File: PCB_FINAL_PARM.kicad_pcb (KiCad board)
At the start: 2 copper layers, 87.6 x 95.2 mm, 48 parts, among them J1 Conn_01x02_Servo1, J10 Conn_01x04_TRIS, J11 Conn_01x04_3v3, J2 Conn_01x03_UART1, J3 Conn_01x03_UART2, J4 Conn_01x04_PWM, J5 Conn_01x05_PROGRAMER, J6 Conn_01x02_POWER, J7 Conn_01x02_Servo2, J8 Conn_01x02_Servo3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

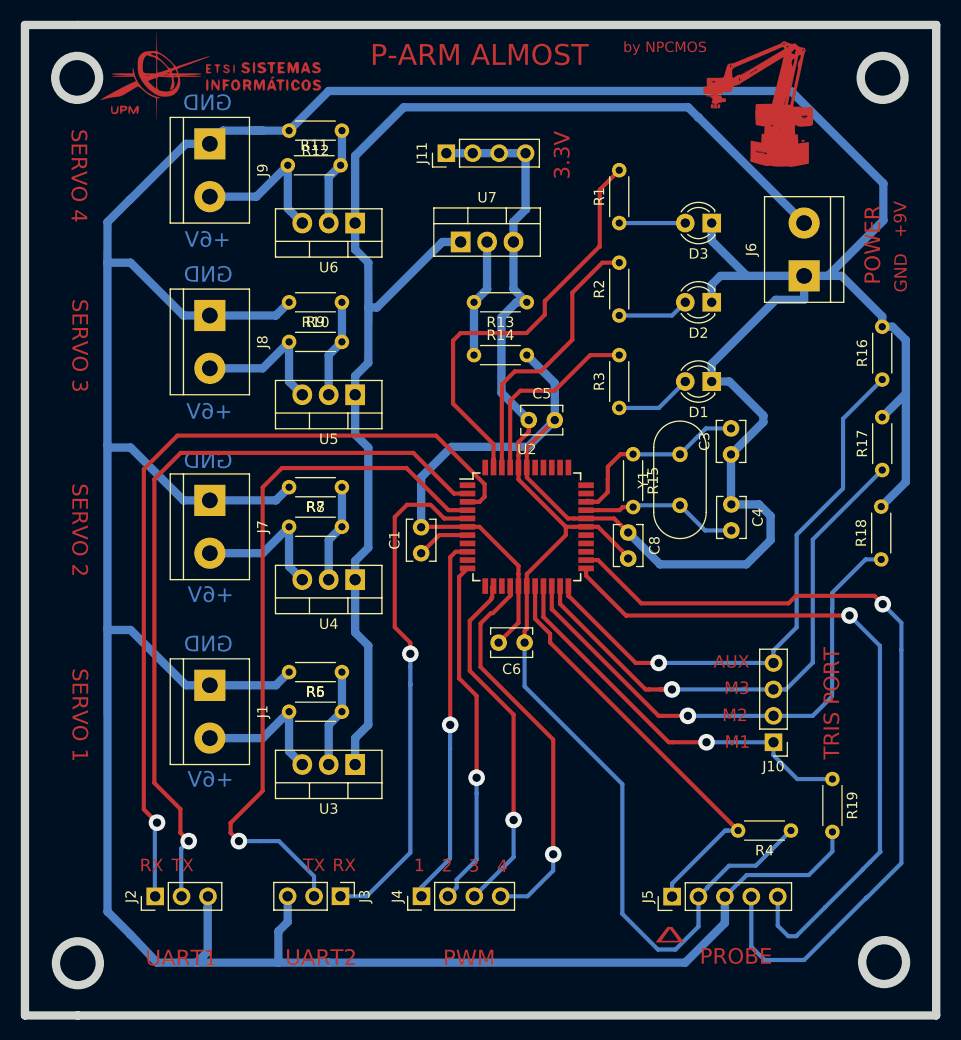
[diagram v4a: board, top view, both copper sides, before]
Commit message: Pasadas comprobaciones de HW y modificaciones con respecto a la sonda
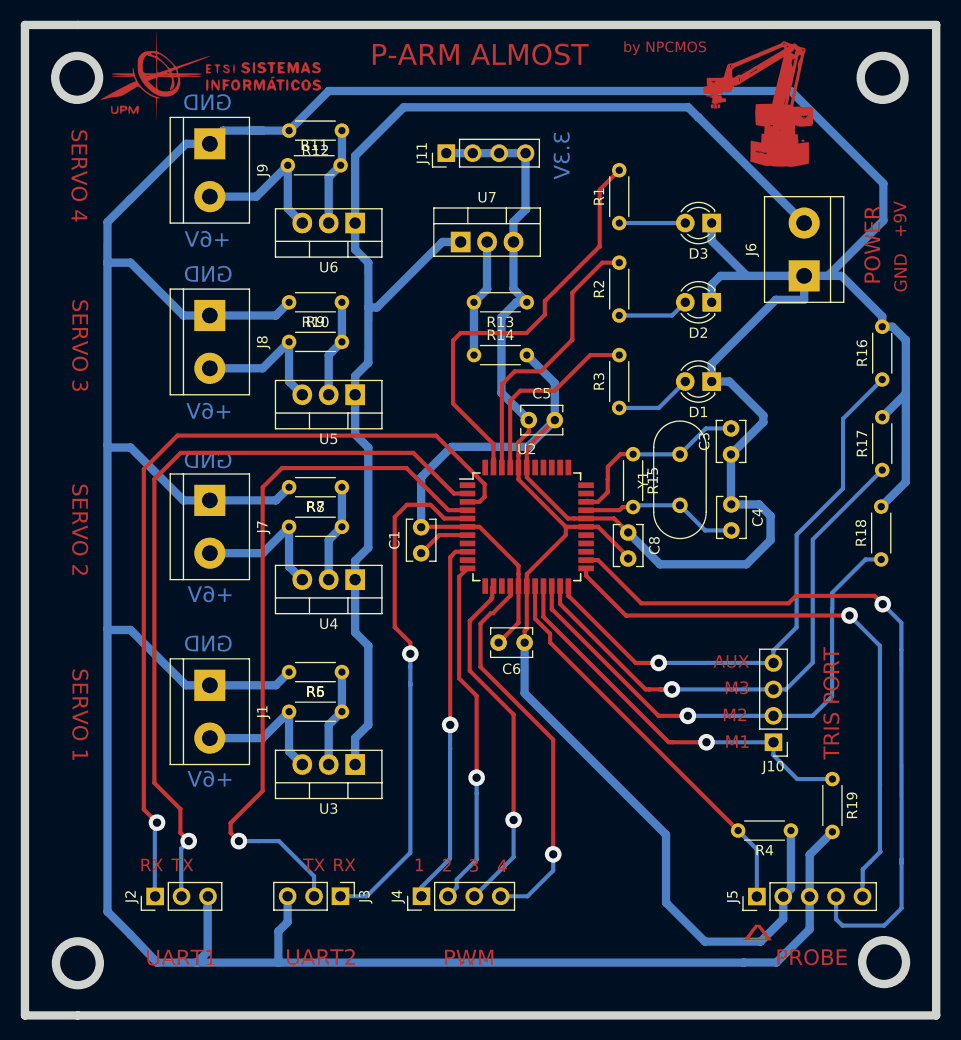
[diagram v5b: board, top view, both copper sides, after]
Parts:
- moved J5 8.15 mm to (205.0, 142.2)
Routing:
- net Net-(J5-Pad5): track 68.1 -> 56.7 mm
- net Net-(J5-Pad4): track 80.4 -> 70.6 mm
- net Net-(J5-Pad1): track 41.3 -> 38.7 mm
- net GND: track 485.7 -> 487.3 mm
- net +3V3: track 123.8 -> 122.9 mm

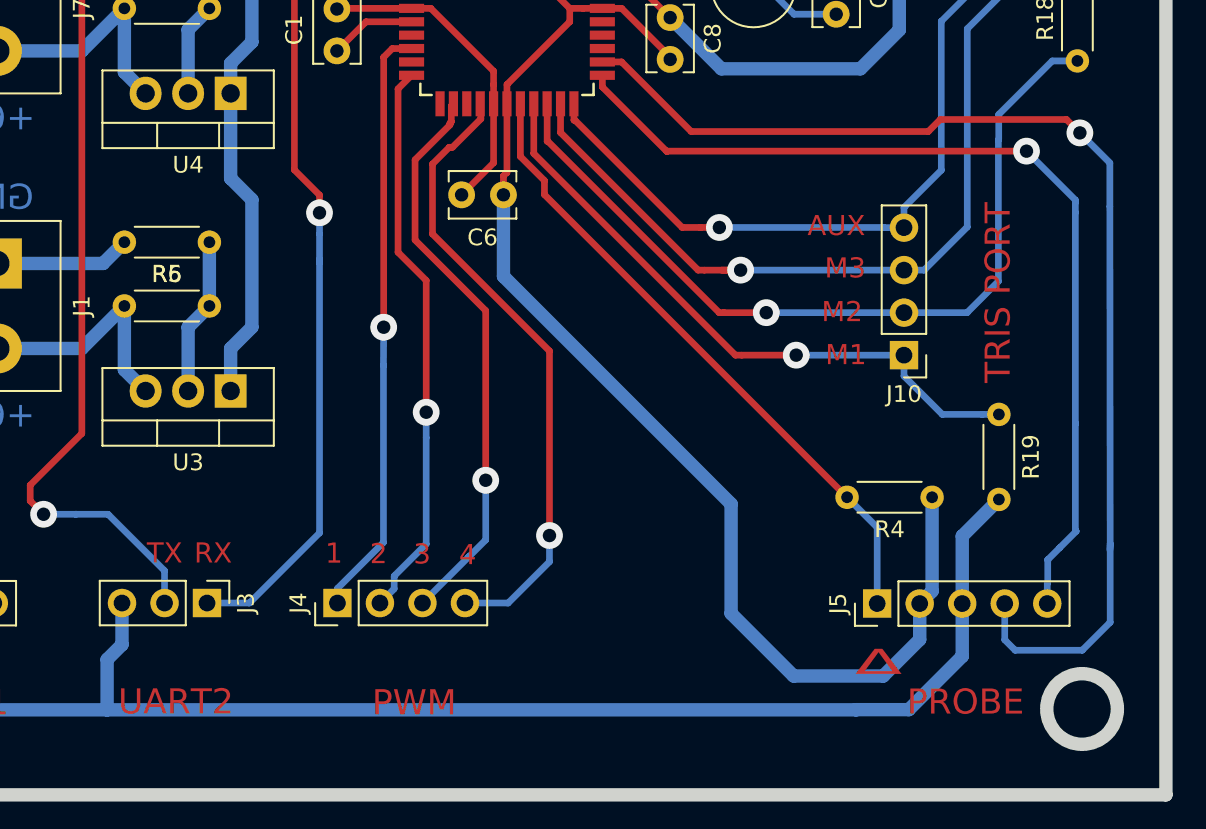
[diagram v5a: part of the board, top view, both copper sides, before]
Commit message: Aumentado el espacio para la sonda
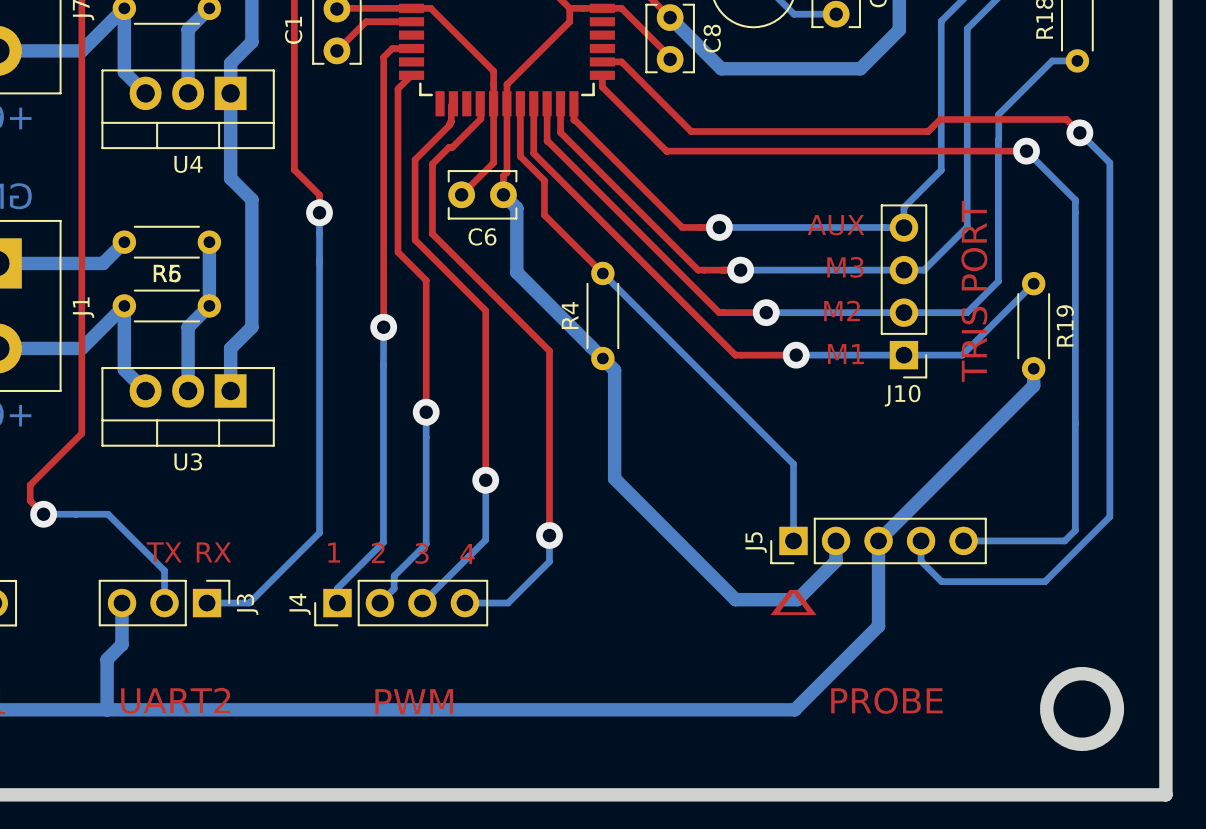
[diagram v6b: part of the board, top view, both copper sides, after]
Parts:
- moved R4 21.3 mm to (188.6, 127.6), turned to 90 degrees
- moved R19 8.08 mm to (214.3, 123.1)
- moved J5 6.24 mm to (200.0, 138.5)
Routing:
- net +3V3: track 122.9 -> 107.9 mm
- net Net-(J5-Pad1): track 38.7 -> 32.9 mm
- net GND: track 487.3 -> 492.0 mm
- net Net-(J5-Pad5): track 56.7 -> 58.5 mm
- net Net-(J10-Pad1): track 38.3 -> 39.9 mm
- net Net-(J5-Pad4): track 70.6 -> 69.2 mm

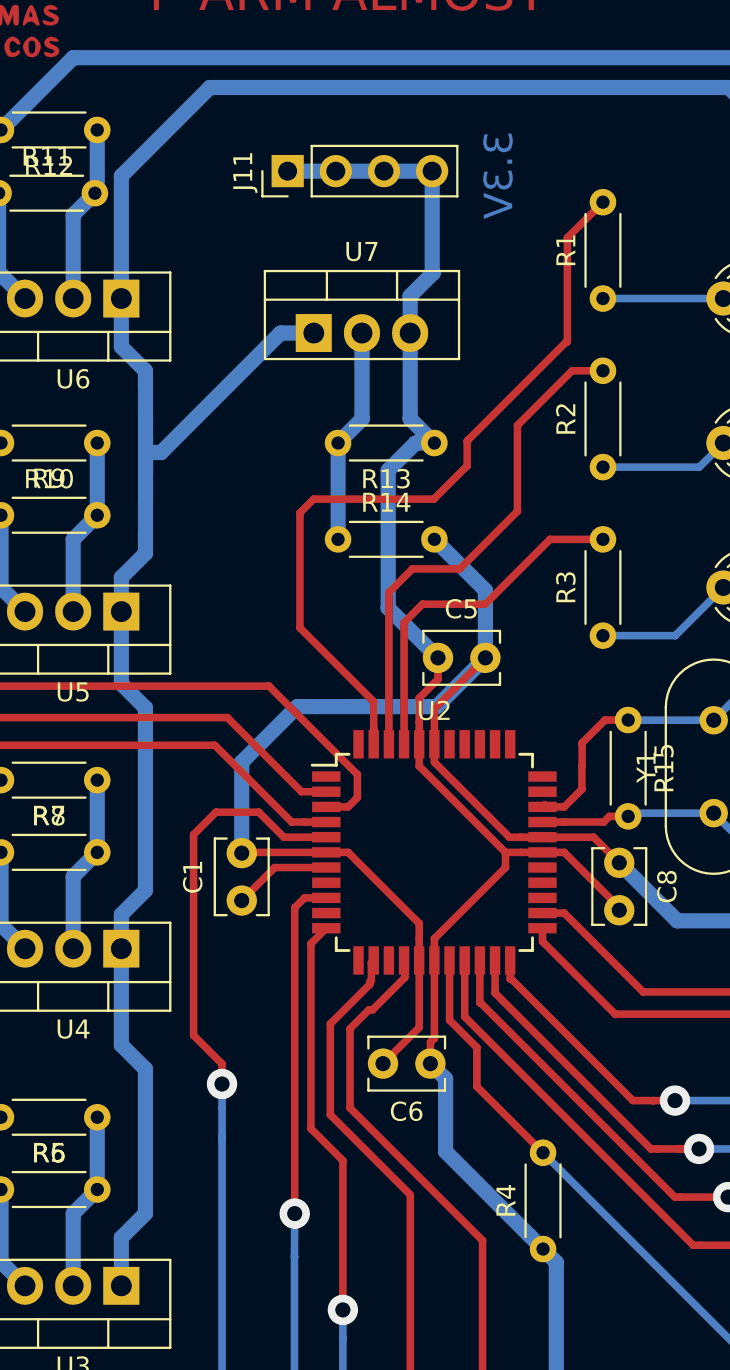
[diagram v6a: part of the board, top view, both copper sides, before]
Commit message: Sustituido el regulador del dspic
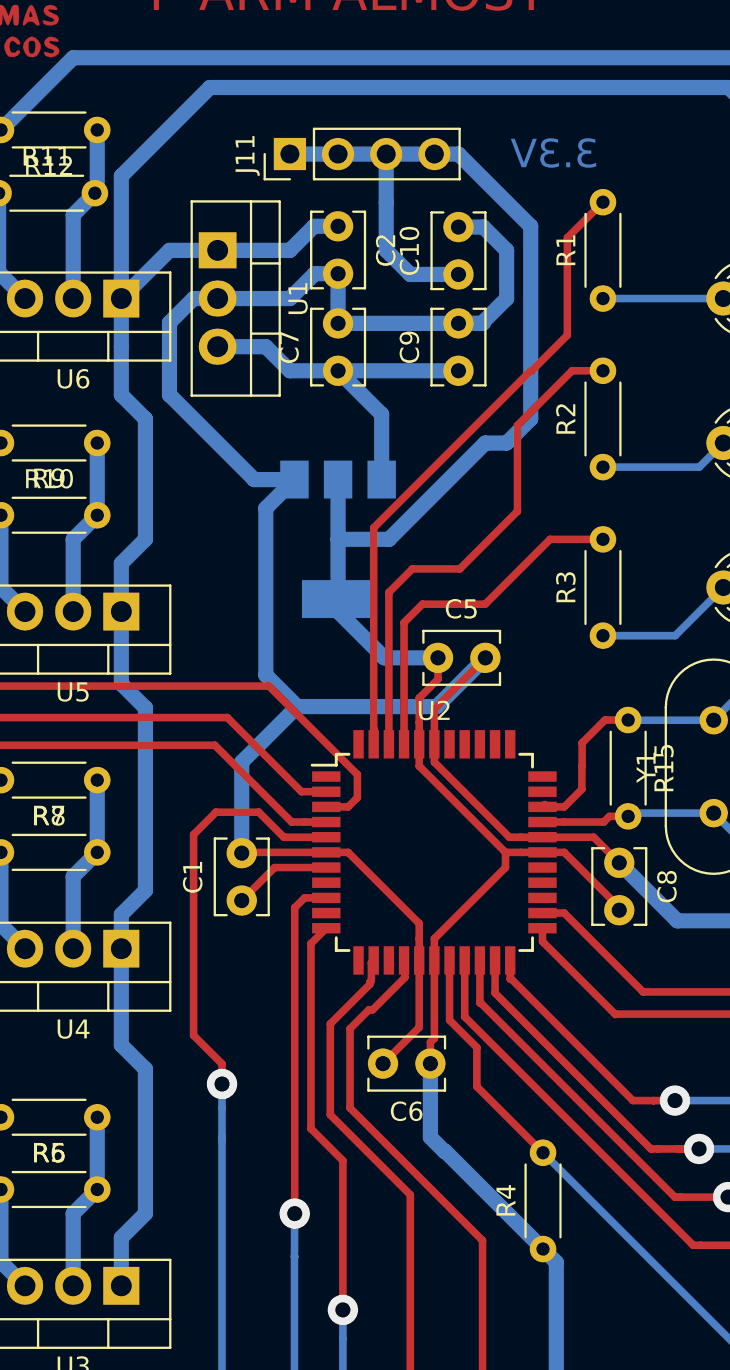
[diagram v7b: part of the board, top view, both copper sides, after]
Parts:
- removed R13: 240, Resistor_THT:R_Axial_DIN0204_L3.6mm_D1.6mm_P5.08mm_Horizontal
- removed R14: 400, Resistor_THT:R_Axial_DIN0204_L3.6mm_D1.6mm_P5.08mm_Horizontal
- added C10: 22uF, Capacitor_THT:C_Disc_D3.8mm_W2.6mm_P2.50mm, F.Cu at (184.2, 76.2)
- added C2: 0.33uF, Capacitor_THT:C_Disc_D3.8mm_W2.6mm_P2.50mm, F.Cu at (177.8, 73.7)
- added C7: 0.1uF, Capacitor_THT:C_Disc_D3.8mm_W2.6mm_P2.50mm, F.Cu at (177.8, 81.3)
- added C9: 10uF, Capacitor_THT:C_Disc_D3.8mm_W2.6mm_P2.50mm, F.Cu at (184.2, 81.3)
- added U1: L7805, Package_TO_SOT_THT:TO-220-3_Vertical, F.Cu at (171.4, 74.9)
- U7: value LM317T/DSPIC -> AZ1117-3.3; footprint Package_TO_SOT_THT:TO-220-3_Vertical -> Package_TO_SOT_SMD:SOT-223-3_TabPin2; moved to B.Cu
- moved U7 11.0 mm to (177.8, 90.2), turned to 270 degrees
- moved J11 0.91 mm to (175.3, 69.8)
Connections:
- J6 pad 2: Net-(J6-Pad2) -> Net-(C2-Pad1)
- U3 pad 1: Net-(J6-Pad2) -> Net-(C2-Pad1)
- U4 pad 1: Net-(J6-Pad2) -> Net-(C2-Pad1)
- U5 pad 1: Net-(J6-Pad2) -> Net-(C2-Pad1)
- U6 pad 1: Net-(J6-Pad2) -> Net-(C2-Pad1)
- U7 pad 1: Net-(J6-Pad2) -> GND
- U7 pad 2: Net-(R13-Pad2) -> +3V3
- U7 pad 3: +3V3 -> Net-(C7-Pad1)
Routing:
- net Net-(C2-Pad1): track 0.00 -> 124.4 mm
- net Net-(J6-Pad2): track 122.9 -> 0.00 mm
- net GND: track 492.0 -> 539.0 mm
- net +3V3: track 107.9 -> 131.3 mm
- net Net-(C7-Pad1): track 0.00 -> 19.9 mm
- net Net-(R13-Pad2): track 11.4 -> 0.00 mm
- net Net-(R1-Pad2): track 41.4 -> 34.5 mm

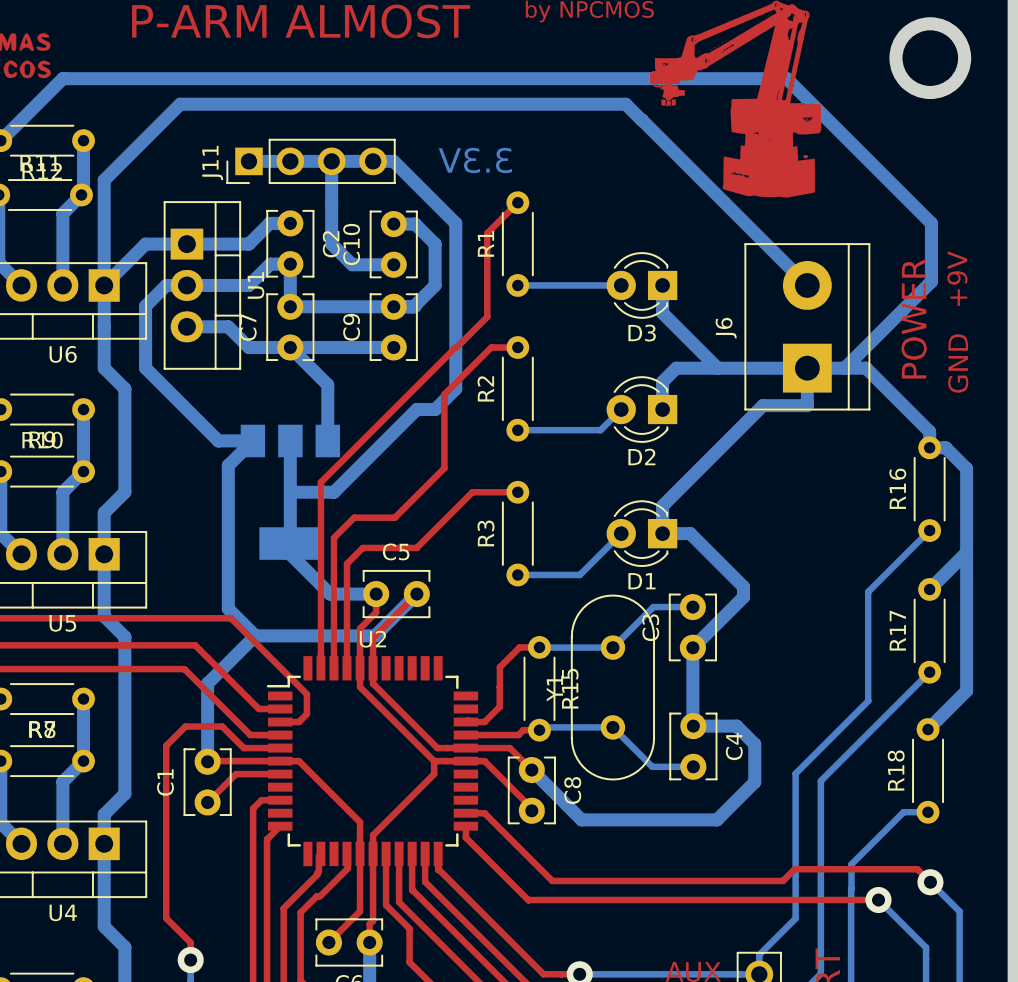
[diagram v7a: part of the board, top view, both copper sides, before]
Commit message: Corregidos los valores de resistencias de los LM317 y alejado el regulador del dspic
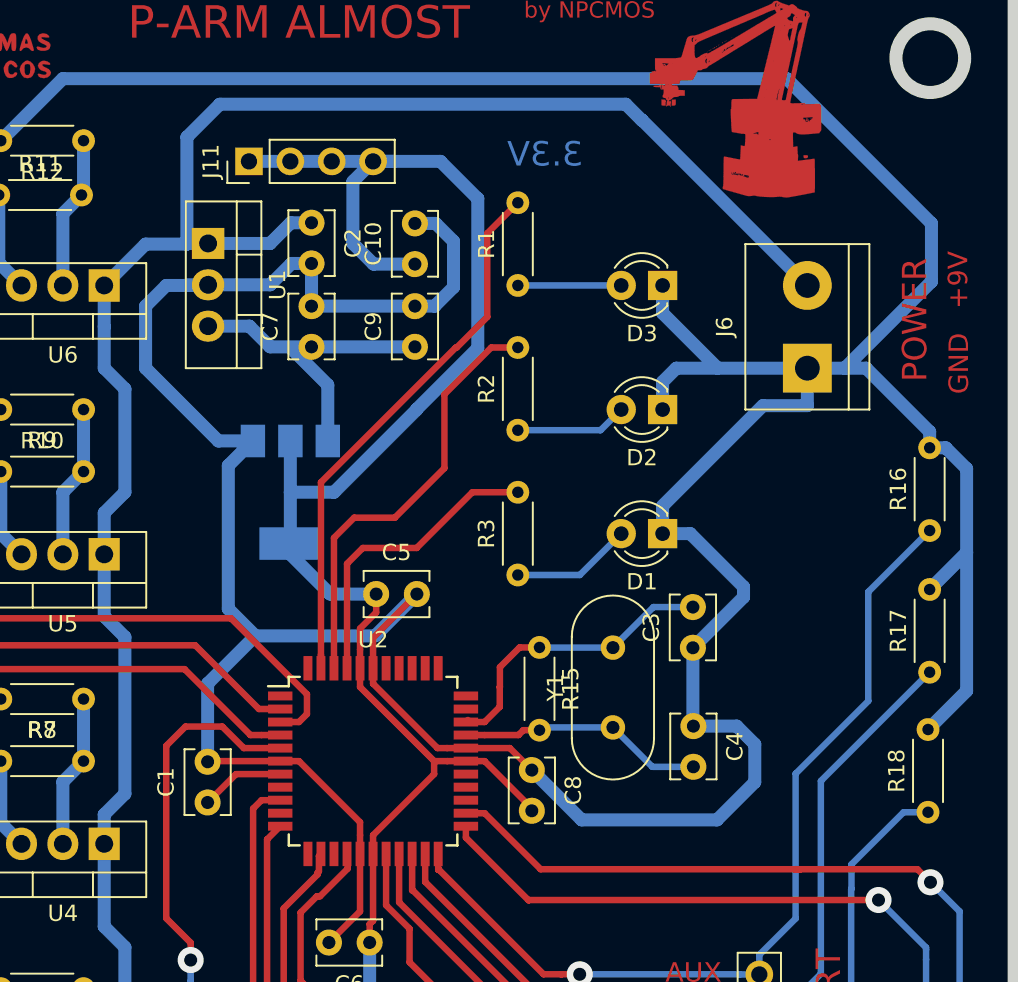
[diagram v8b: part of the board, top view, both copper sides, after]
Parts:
- R10, R12, R6, R8: value 910 -> 500
- R11, R5, R7, R9: value 240 -> 150
- moved U1 1.30 mm to (172.8, 74.9)
- moved C10 1.30 mm to (185.4, 76.2)
- moved C7 1.30 mm to (179.1, 81.2)
- moved C9 1.30 mm to (185.4, 81.2)
- moved C2 1.30 mm to (179.1, 73.6)
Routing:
- net Net-(C2-Pad1): track 124.4 -> 119.7 mm
- net +3V3: track 131.3 -> 135.2 mm
- net GND: track 539.0 -> 540.1 mm
